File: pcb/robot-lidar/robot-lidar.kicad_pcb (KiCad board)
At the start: 2 copper layers, 100 x 100 mm, 33 parts, among them J1 Conn_ARM_SWD_TagConnect_TC2030, J12 Conn_02x20_Odd_Even, J2 YLIDAR X4, J3 Jack-DC, J4 Conn_02x03_Odd_Even, J5 Conn_01x02, J6 Conn_01x02, J7 Conn_01x02, J8 Conn_01x02, U1 STM32F103C8Tx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

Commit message: wiring pca
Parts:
- removed C14, C15: 0.1uF, Capacitor_SMD:C_0603_1608Metric
- removed J1: Conn_ARM_SWD_TagConnect_TC2030, Connector_PinHeader_2.54mm:PinHeader_1x06_P2.54mm_Vertical
- removed J4: Conn_02x03_Odd_Even, Connector_PinHeader_2.54mm:PinHeader_2x03_P2.54mm_Vertical_SMD
- removed R4, R5, R6: 10k, Resistor_SMD:R_0603_1608Metric
- removed Y1: Crystal, Crystal:Crystal_SMD_HC49-SD
- R3: value 10k -> R_Small
- U1: value STM32F103C8Tx -> PCA9635; footprint Package_QFP:LQFP-48_7x7mm_P0.5mm -> Package_SO:TSSOP-28_4.4x9.7mm_P0.65mm
- moved R3 18.9 mm to (104.5, 101.7)
- moved U1 2.26 mm to (99.7, 98.0), turned to -45 degrees
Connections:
- R3 pad 1: +3V3 -> GND
- R3 pad 2: Net-(J4-Pin_1) -> Net-(U1-~{OE})
- U1 pad 1: +3.3V -> GND
- U1 pad 10: unconnected-(U1-PA0-Pad10) -> MOTOR_3_A
- U1 pad 11: unconnected-(U1-PA1-Pad11) -> MOTOR_3_B
- U1 pad 12: unconnected-(U1-PA2-Pad12) -> MOTOR_4_A
- U1 pad 13: unconnected-(U1-PA3-Pad13) -> MOTOR_4_B
- U1 pad 14: unconnected-(U1-PA4-Pad14) -> GND
- U1 pad 16: MOTOR_1_A -> unconnected-(U1-LED9-Pad16)
- U1 pad 17: MOTOR_1_B -> unconnected-(U1-LED10-Pad17)
- U1 pad 18: MOTOR_2_B -> unconnected-(U1-LED11-Pad18)
- U1 pad 19: MOTOR_2_A -> unconnected-(U1-LED12-Pad19)
- U1 pad 2: unconnected-(U1-PC13-Pad2) -> GND
- U1 pad 20: BOOT1 -> unconnected-(U1-LED13-Pad20)
- U1 pad 21: SCL -> unconnected-(U1-LED14-Pad21)
- U1 pad 22: SDA -> unconnected-(U1-LED15-Pad22)
- U1 pad 23: GND -> Net-(U1-~{OE})
- U1 pad 24: +3.3V -> GND
- U1 pad 25: unconnected-(U1-PB12-Pad25) -> GND
- U1 pad 26: unconnected-(U1-PB13-Pad26) -> SCL
- U1 pad 27: unconnected-(U1-PB14-Pad27) -> SDA
- U1 pad 28: unconnected-(U1-PB15-Pad28) -> +5V
- U1 pad 3: unconnected-(U1-PC14-Pad3) -> GND
- U1 pad 4: unconnected-(U1-PC15-Pad4) -> GND
- U1 pad 5: PH0 -> GND
- U1 pad 6: PH1 -> MOTOR_2_A
- U1 pad 7: RESET -> MOTOR_2_B
- U1 pad 8: GND -> MOTOR_1_B
- U1 pad 9: +3.3V -> MOTOR_1_A
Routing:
- net +3V3: track 175.9 -> 72.8 mm, vias 34 -> 31
- net PA13-SWDIO: track 59.3 -> 0.00 mm, vias 4 -> 0
- net PB3-SWO: track 54.4 -> 0.00 mm, vias 1 -> 0
- net PA14-SWCLK: track 52.9 -> 0.00 mm, vias 2 -> 0
- net RESET: track 46.2 -> 0.00 mm, vias 2 -> 0
- net +3.3V: track 25.3 -> 0.00 mm, vias 3 -> 0
- net BOOT0: track 22.1 -> 0.00 mm, vias 2 -> 0
- net BOOT1: track 18.1 -> 0.00 mm, vias 2 -> 0
- net +5V: track 286.4 -> 303.0 mm
- net Net-(J4-Pin_5): track 13.9 -> 0.00 mm
- net PH1: track 12.4 -> 0.00 mm
- net PH0: track 12.2 -> 0.00 mm
- net Net-(J4-Pin_6): track 11.4 -> 0.00 mm
- net GND: track 19.7 -> 10.4 mm, vias 56 -> 55
- net Net-(J4-Pin_2): track 5.32 -> 0.00 mm
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
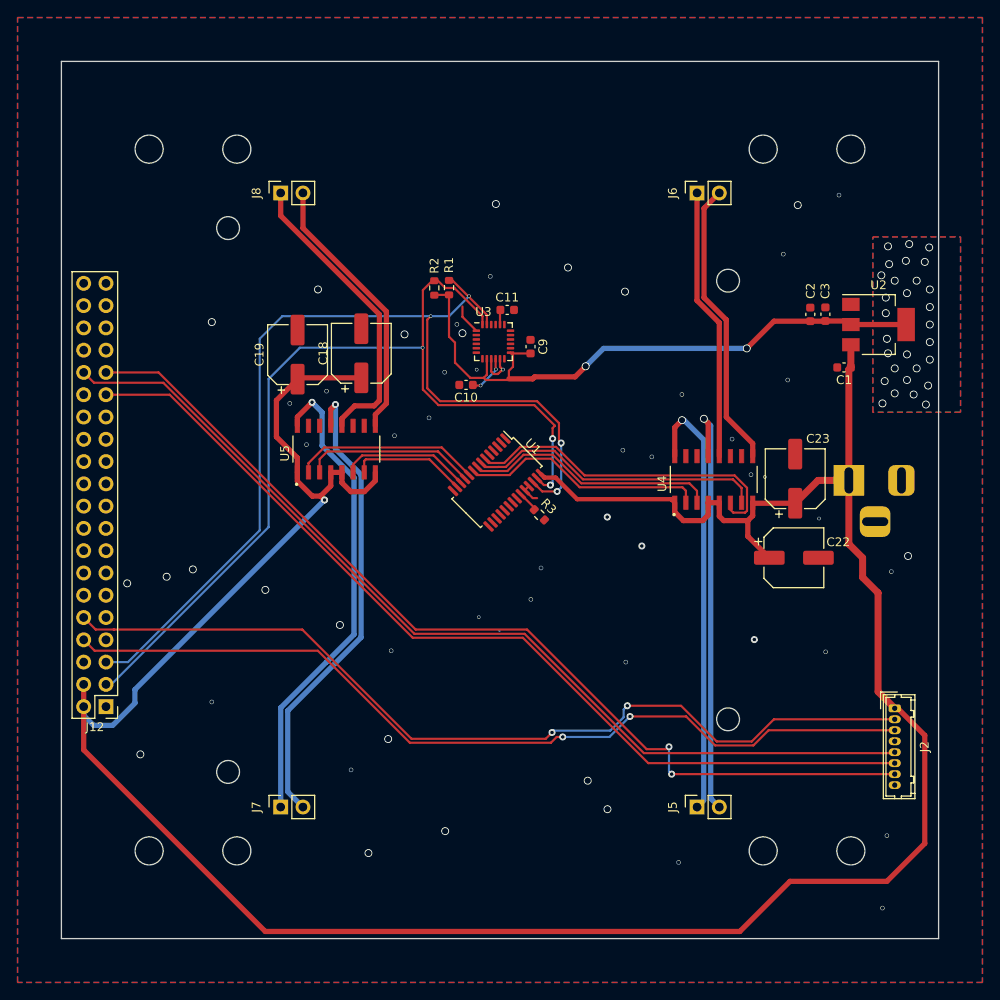
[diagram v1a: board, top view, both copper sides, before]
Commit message: wiring atmega and resize board
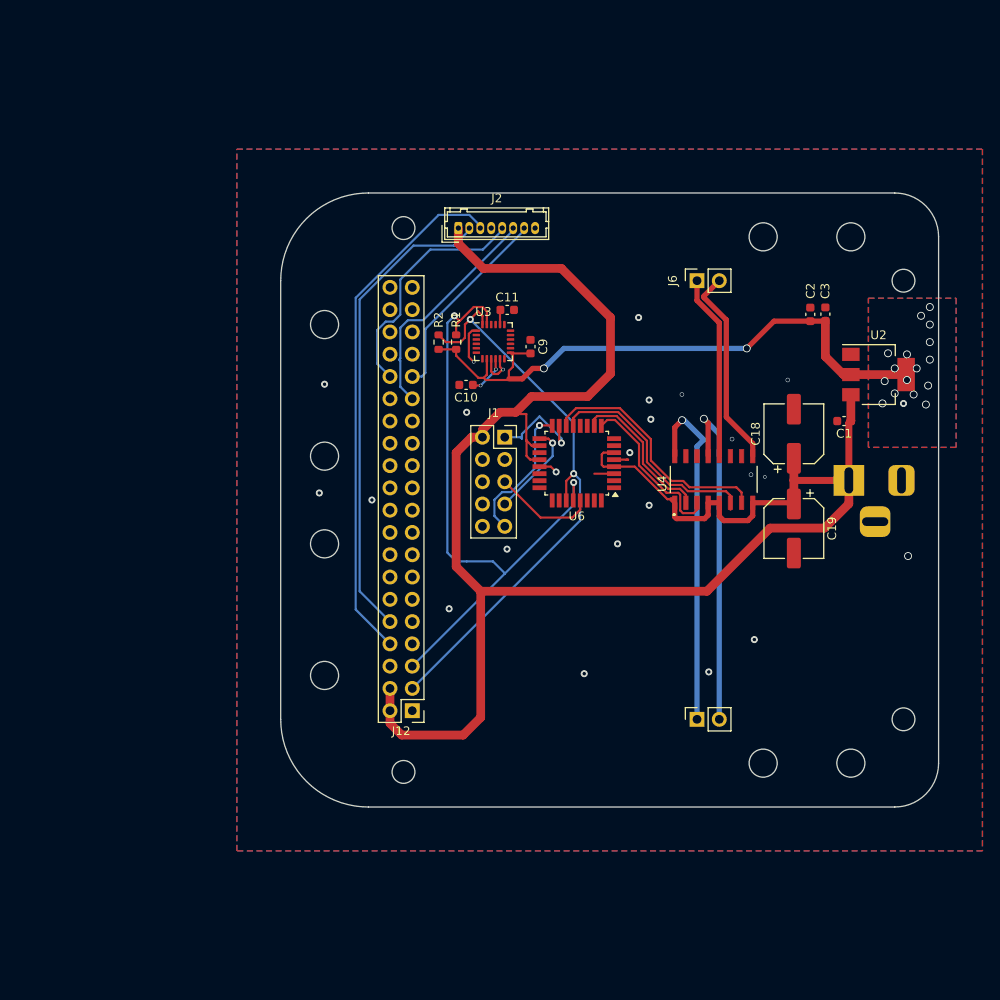
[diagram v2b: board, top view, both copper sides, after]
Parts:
- removed C22, C23: C_Polarized_Small, Capacitor_SMD:CP_Elec_6.3x4.9
- removed J7, J8: Conn_01x02, Connector_PinSocket_2.54mm:PinSocket_1x02_P2.54mm_Vertical
- removed R3: R_Small, Resistor_SMD:R_0603_1608Metric
- removed U1: PCA9635, Package_SO:TSSOP-28_4.4x9.7mm_P0.65mm
- removed U5: MX1508, MX1508:SOIC127P600X177-16N
- added J1: AVR-ISP-10, Connector_PinSocket_2.54mm:PinSocket_2x05_P2.54mm_Vertical, F.Cu at (100.5, 92.8)
- added U6: ATmega328P-A, Package_QFP:TQFP-32_7x7mm_P0.8mm, F.Cu at (108.8, 95.8)
- moved J2 74.0 mm to (95.2, 69.0), turned to 0 degrees
- moved C19 59.9 mm to (133.5, 103.2), turned to -90 degrees
- moved C18 50.2 mm to (133.5, 92.5)
- moved J12 34.9 mm to (90.0, 124.0)
- moved J5 10.0 mm to (122.5, 125.0)
- moved J6 10.0 mm to (122.5, 75.0)
- moved R1 6.26 mm to (95.0, 82.0)
- moved R2 6.19 mm to (93.0, 82.0)
- moved C1 6.11 mm to (139.2, 91.0)
- moved U2 5.70 mm to (143.2, 85.7)
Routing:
- net +5V: track 303.0 -> 210.7 mm, vias 1 -> 0
- net M_EN: track 110.9 -> 22.8 mm, vias 2 -> 0
- net M_SCTR: track 110.5 -> 27.4 mm
- net DEV_EN: track 107.3 -> 26.5 mm
- net Net-(J7-Pin_1): track 55.0 -> 0.00 mm, vias 1 -> 0
- net Net-(J7-Pin_2): track 53.9 -> 0.00 mm, vias 1 -> 0
- net UART_RX: track 103.0 -> 54.2 mm, vias 2 -> 0
- net SCL: track 114.8 -> 73.6 mm, vias 4 -> 2
- net SDA: track 108.7 -> 67.5 mm, vias 3 -> 2
- net UART_TX: track 100.6 -> 60.0 mm, vias 2 -> 0
- net Net-(J8-Pin_1): track 34.3 -> 0.00 mm
- net Net-(J8-Pin_2): track 31.0 -> 0.00 mm
- net MOTOR_3_A: track 21.4 -> 0.00 mm
- net MOTOR_3_B: track 19.8 -> 0.00 mm
- net MISO: track 0.00 -> 16.2 mm, vias 0 -> 1
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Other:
- board size 100 x 100 mm -> 75 x 70 mm
